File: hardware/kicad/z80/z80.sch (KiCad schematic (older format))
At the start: 1 part, among them U1 Z80CPU

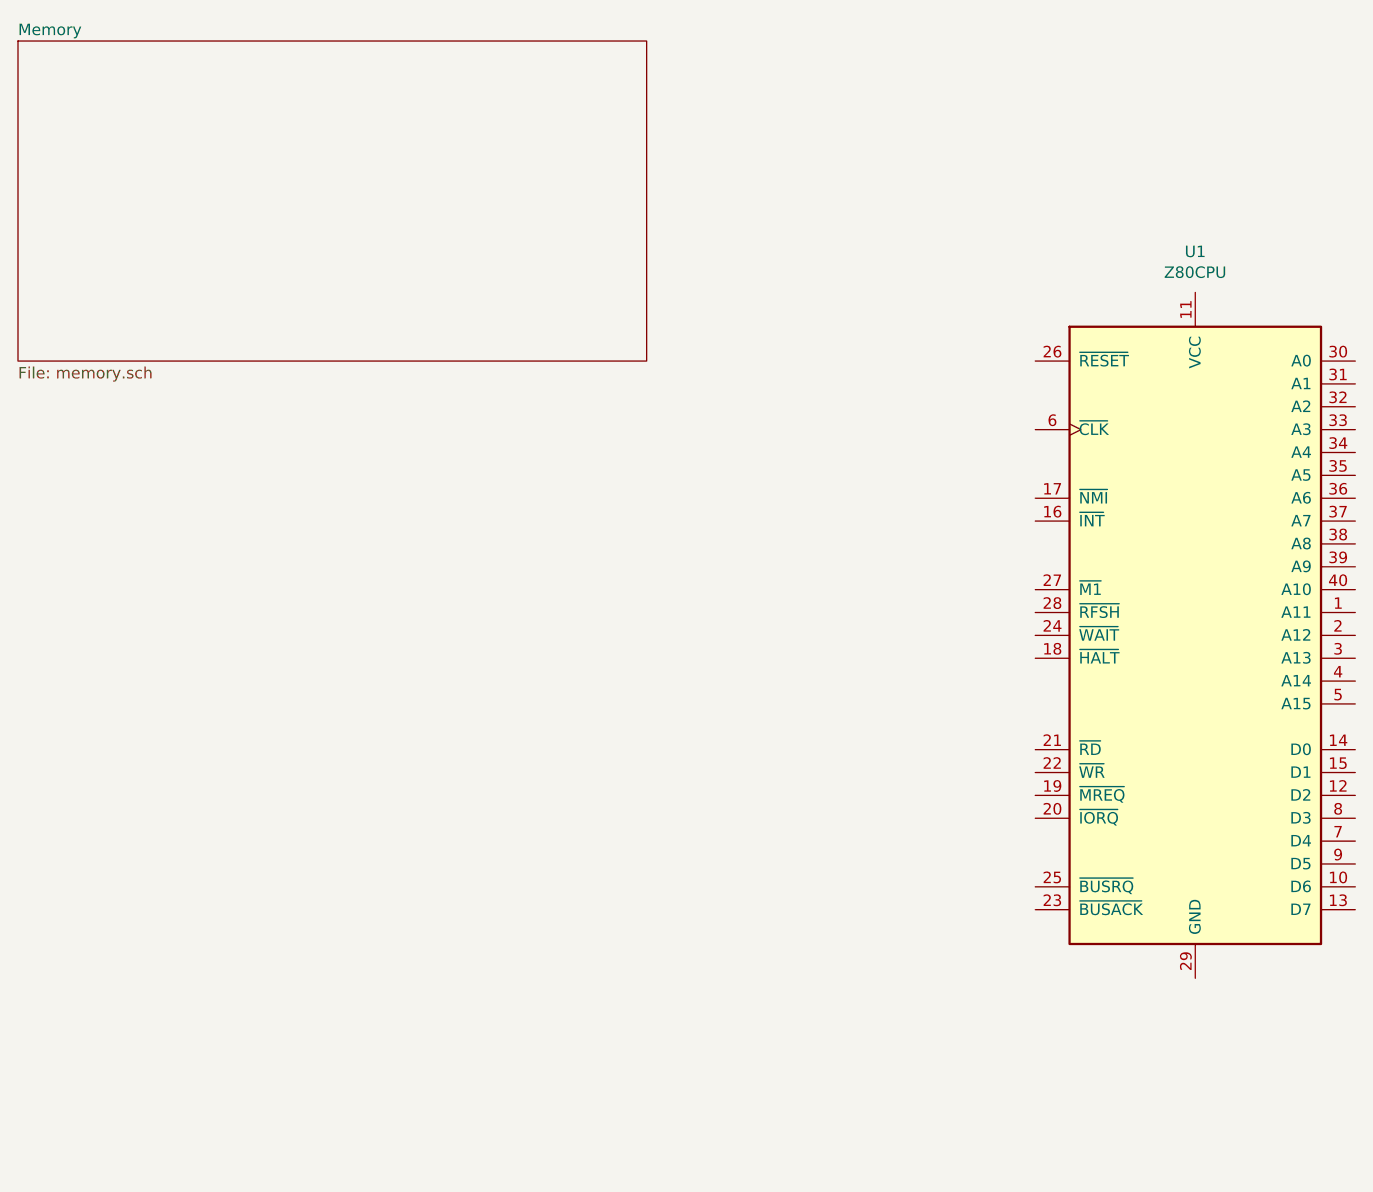
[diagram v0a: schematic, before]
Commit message: Adding more baseline schematics and notes
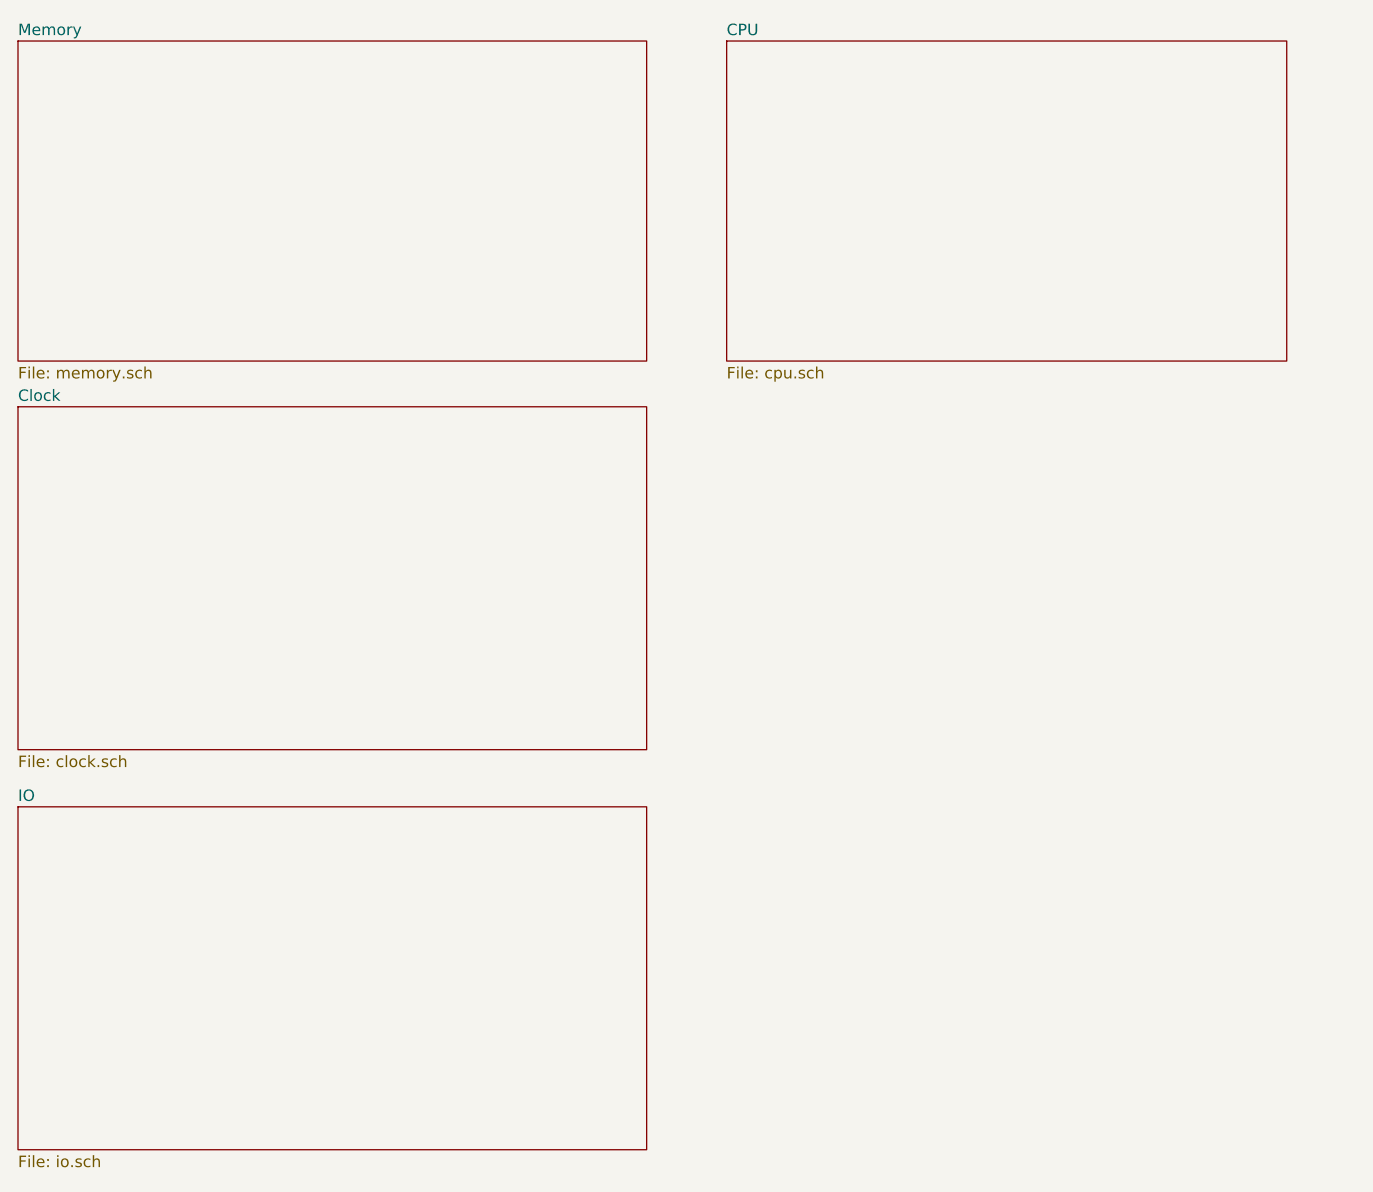
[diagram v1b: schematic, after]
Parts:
- removed U1: Z80CPU, symbol CPU:Z80CPU
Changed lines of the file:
@@
 EESchema Schematic File Version 4
+LIBS:z80-cache
 EELAYER 26 0
 EELAYER END
 $Descr A4 11693 8268
 encoding utf-8
-Sheet 1 2
+Sheet 1 5
 Title ""
 Date ""
@@
 Comment4 ""
 $EndDescr
-$Comp
-L CPU:Z80CPU U1
-U 1 1 66E7ACE6
-P 6000 3550
-F 0 "U1" H 6000 5228 50  0000 C CNN
-F 1 "Z80CPU" H 6000 5137 50  0000 C CNN
-F 2 "" H 6000 3950 50  0001 C CNN
-F 3 "www.zilog.com/manage_directlink.php?filepath=docs/z80/um0080" H 6000 3950 50  0001 C CNN
-	1    6000 3550
-	1    0    0    -1
-$EndComp
 $Sheet
 S 850  950  2750 1400
@@
 F1 "memory.sch" 50
 $EndSheet
+$Sheet
+S 850  2550 2750 1500
+U 66E7AE3D
+F0 "Clock" 50
+F1 "clock.sch" 50
+$EndSheet
+$Sheet
+S 850  4300 2750 1500
+U 66E7B429
+F0 "IO" 50
+F1 "io.sch" 50
+$EndSheet
+$Sheet
+S 3950 950  2450 1400
+U 66EB480F
+F0 "CPU" 50
+F1 "cpu.sch" 50
+$EndSheet
 $EndSCHEMATC
